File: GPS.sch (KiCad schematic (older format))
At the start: 6 parts, among them U5 MAX-M8

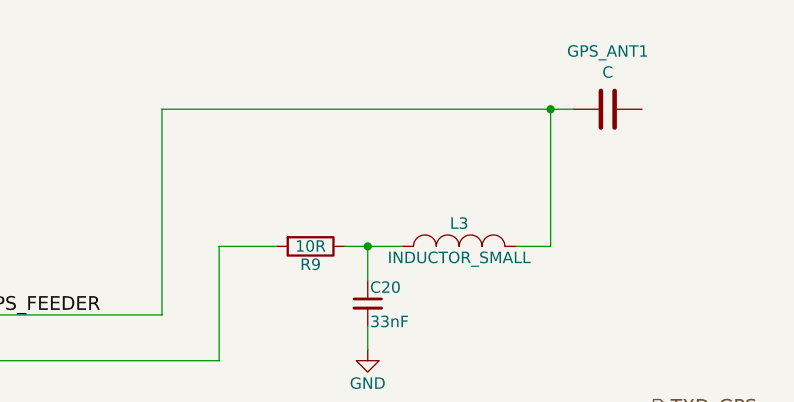
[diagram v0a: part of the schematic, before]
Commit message: Added edge-mount SMAs
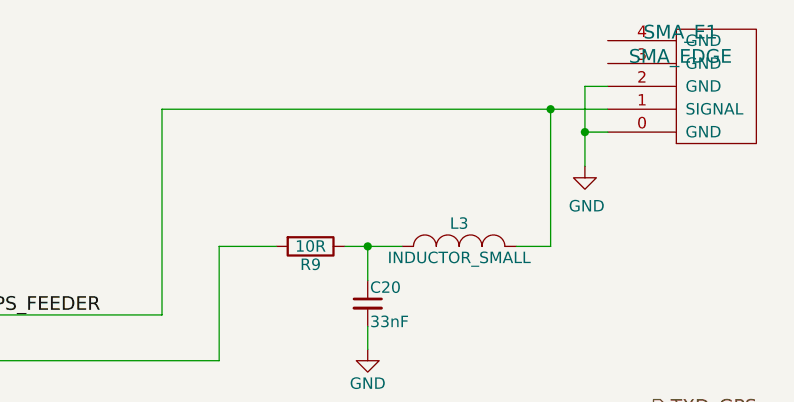
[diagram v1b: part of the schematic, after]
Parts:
- removed GPS_ANT1: C, Capacitors_SMD:C_1206, symbol C
- added SMA_E1: SMA_EDGE, SMA_EDGE:SMA_EDGE, symbol SMA_EDGE
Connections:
- net GND: now also SMA_E1.0 (GND), SMA_E1.2 (GND)
- net GPS_FEEDER: now also SMA_E1.1 (SIGNAL)
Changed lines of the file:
@@
 LIBS:miniultrapro
 LIBS:texas-instruments
+LIBS:sma_edge
 LIBS:lorawan_gps-cache
 EELAYER 25 0
@@
 	1    0    0    -1
 $EndComp
-$Comp
-L C GPS_ANT1
-U 1 1 56DB5A9C
-P 7050 2600
-F 0 "GPS_ANT1" V 6797 2600 50  0000 C CNN
-F 1 "C" V 6889 2600 50  0000 C CNN
-F 2 "Capacitors_SMD:C_1206" H 7088 2450 50  0001 C CNN
-F 3 "" H 7050 2600 50  0000 C CNN
-F 4 "1575AT43A40" V 7050 2600 60  0001 C CNN "MPN"
-	1    7050 2600
-	0    1    1    0
-$EndComp
 Text Label 4300 3500 0    60   ~ 0
 GPS_FEEDER
 $Comp
-L GND #PWR032
+L GND #PWR033
 U 1 1 56E9952A
 P 2700 5250
-F 0 "#PWR032" H 2700 5000 50  0001 C CNN
+F 0 "#PWR033" H 2700 5000 50  0001 C CNN
 F 1 "GND" H 2700 5100 50  0000 C CNN
 F 2 "" H 2700 5250 50  0000 C CNN
@@
 	1    0    0    -1
 $EndComp
-Wire Wire Line
-	2700 4700 2950 4700
-Wire Wire Line
-	2700 4650 2700 5250
-Wire Wire Line
-	2950 4800 2700 4800
-Connection ~ 2700 4800
-Wire Wire Line
-	2950 4900 2700 4900
-Connection ~ 2700 4900
 NoConn ~ 4250 4500
 NoConn ~ 4250 4900
@@
 NoConn ~ 2950 4150
 $Comp
-L +3.3V #PWR033
+L +3.3V #PWR034
 U 1 1 56E99604
 P 2700 3200
-F 0 "#PWR033" H 2700 3050 50  0001 C CNN
+F 0 "#PWR034" H 2700 3050 50  0001 C CNN
 F 1 "+3.3V" H 2700 3340 50  0000 C CNN
 F 2 "" H 2700 3200 50  0000 C CNN
@@
 	1    0    0    -1
 $EndComp
-Wire Wire Line
-	2700 4350 2950 4350
-Wire Wire Line
-	2700 3200 2700 4350
-Wire Wire Line
-	2950 3500 2700 3500
-Connection ~ 2700 3500
-Wire Wire Line
-	2950 3600 2700 3600
-Connection ~ 2700 3600
-Wire Wire Line
-	2950 3800 2700 3800
-Connection ~ 2700 3800
 $Comp
 L R R9
@@
 $EndComp
 $Comp
-L GND #PWR034
+L GND #PWR035
 U 1 1 56E99D41
 P 6000 3650
-F 0 "#PWR034" H 6000 3400 50  0001 C CNN
+F 0 "#PWR035" H 6000 3400 50  0001 C CNN
 F 1 "GND" H 6000 3500 50  0000 C CNN
 F 2 "" H 6000 3650 50  0000 C CNN
@@
 	1    0    0    -1
 $EndComp
-Connection ~ 2700 4350
-Connection ~ 2700 4700
-Wire Wire Line
-	4250 3500 5100 3500
-Wire Wire Line
-	5100 3500 5100 2600
-Wire Wire Line
-	5100 2600 6900 2600
-Wire Wire Line
-	6650 3200 6800 3200
-Wire Wire Line
-	6800 3200 6800 2600
-Connection ~ 6800 2600
-Wire Wire Line
-	5900 3200 6150 3200
-Wire Wire Line
-	5600 3200 5350 3200
-Wire Wire Line
-	5350 3200 5350 3700
-Wire Wire Line
-	5350 3700 4250 3700
-Wire Wire Line
-	6000 3350 6000 3200
-Connection ~ 6000 3200
-Wire Wire Line
-	6000 3650 6000 3550
-Wire Wire Line
-	4250 3900 7250 3900
-Wire Wire Line
-	4250 4000 7250 4000
-Wire Wire Line
-	4250 4200 7250 4200
-Wire Wire Line
-	4250 4300 7250 4300
 Text HLabel 7250 3900 2    60   Output ~ 0
 TXD_GPS
@@
 Text HLabel 7250 4300 2    60   Input ~ 0
 SCL_GPS
+$Comp
+L SMA_EDGE SMA_E1
+U 1 1 56F50EC5
+P 7400 2600
+F 0 "SMA_E1" H 7368 2263 60  0000 C CNN
+F 1 "SMA_EDGE" H 7368 2369 60  0000 C CNN
+F 2 "SMA_EDGE:SMA_EDGE" H 7400 2600 60  0001 C CNN
+F 3 "" H 7400 2600 60  0000 C CNN
+	1    7400 2600
+	1    0    0    1
+$EndComp
+Wire Wire Line
+	2700 4700 2950 4700
+Wire Wire Line
+	2700 4650 2700 5250
+Wire Wire Line
+	2950 4800 2700 4800
+Connection ~ 2700 4800
+Wire Wire Line
+	2950 4900 2700 4900
+Connection ~ 2700 4900
+Wire Wire Line
+	2700 4350 2950 4350
+Wire Wire Line
+	2700 3200 2700 4350
+Wire Wire Line
+	2950 3500 2700 3500
+Connection ~ 2700 3500
+Wire Wire Line
+	2950 3600 2700 3600
+Connection ~ 2700 3600
+Wire Wire Line
+	2950 3800 2700 3800
+Connection ~ 2700 3800
+Connection ~ 2700 4350
+Connection ~ 2700 4700
+Wire Wire Line
+	4250 3500 5100 3500
+Wire Wire Line
+	5100 3500 5100 2600
+Wire Wire Line
+	5100 2600 7050 2600
+Wire Wire Line
+	6650 3200 6800 3200
+Wire Wire Line
+	6800 3200 6800 2600
+Connection ~ 6800 2600
+Wire Wire Line
+	5900 3200 6150 3200
+Wire Wire Line
+	5600 3200 5350 3200
+Wire Wire Line
+	5350 3200 5350 3700
+Wire Wire Line
+	5350 3700 4250 3700
+Wire Wire Line
+	6000 3350 6000 3200
+Connection ~ 6000 3200
+Wire Wire Line
+	6000 3650 6000 3550
+Wire Wire Line
+	4250 3900 7250 3900
+Wire Wire Line
+	4250 4000 7250 4000
+Wire Wire Line
+	4250 4200 7250 4200
+Wire Wire Line
+	4250 4300 7250 4300
+$Comp
+L GND #PWR036
+U 1 1 56F511BA
+P 6950 2850
+F 0 "#PWR036" H 6950 2600 50  0001 C CNN
+F 1 "GND" H 6958 2676 50  0000 C CNN
+F 2 "" H 6950 2850 50  0000 C CNN
+F 3 "" H 6950 2850 50  0000 C CNN
+	1    6950 2850
+	1    0    0    -1
+$EndComp
+Wire Wire Line
+	7050 2500 6950 2500
+Wire Wire Line
+	6950 2500 6950 2850
+Wire Wire Line
+	7050 2700 6950 2700
+Connection ~ 6950 2700
 $EndSCHEMATC

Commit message: Changed L3 to 0603, L2 to 3x3, Fixed P8 silk and made gerbers
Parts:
- L3: footprint Capacitors_SMD:C_0805 -> Capacitors_SMD:C_0603
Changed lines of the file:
@@
 GPS_FEEDER
 $Comp
-L GND #PWR34
+L GND #PWR034
 U 1 1 56E9952A
 P 2700 5250
-F 0 "#PWR34" H 2700 5000 50  0001 C CNN
+F 0 "#PWR034" H 2700 5000 50  0001 C CNN
 F 1 "GND" H 2700 5100 50  0000 C CNN
 F 2 "" H 2700 5250 50  0000 C CNN
@@
 NoConn ~ 2950 4150
 $Comp
-L +3.3V #PWR33
+L +3.3V #PWR035
 U 1 1 56E99604
 P 2700 3200
-F 0 "#PWR33" H 2700 3050 50  0001 C CNN
+F 0 "#PWR035" H 2700 3050 50  0001 C CNN
 F 1 "+3.3V" H 2700 3340 50  0000 C CNN
 F 2 "" H 2700 3200 50  0000 C CNN
@@
 F 0 "L3" H 6400 3300 50  0000 C CNN
 F 1 "INDUCTOR_SMALL" H 6400 3150 50  0000 C CNN
-F 2 "Capacitors_SMD:C_0805" H 6400 3200 50  0001 C CNN
+F 2 "Capacitors_SMD:C_0603" H 6400 3200 50  0001 C CNN
 F 3 "" H 6400 3200 50  0000 C CNN
 	1    6400 3200
@@
 $EndComp
 $Comp
-L GND #PWR35
+L GND #PWR036
 U 1 1 56E99D41
 P 6000 3650
-F 0 "#PWR35" H 6000 3400 50  0001 C CNN
+F 0 "#PWR036" H 6000 3400 50  0001 C CNN
 F 1 "GND" H 6000 3500 50  0000 C CNN
 F 2 "" H 6000 3650 50  0000 C CNN
@@
 	4250 4300 7250 4300
 $Comp
-L GND #PWR36
+L GND #PWR037
 U 1 1 56F511BA
 P 6950 2850
-F 0 "#PWR36" H 6950 2600 50  0001 C CNN
+F 0 "#PWR037" H 6950 2600 50  0001 C CNN
 F 1 "GND" H 6958 2676 50  0000 C CNN
 F 2 "" H 6950 2850 50  0000 C CNN

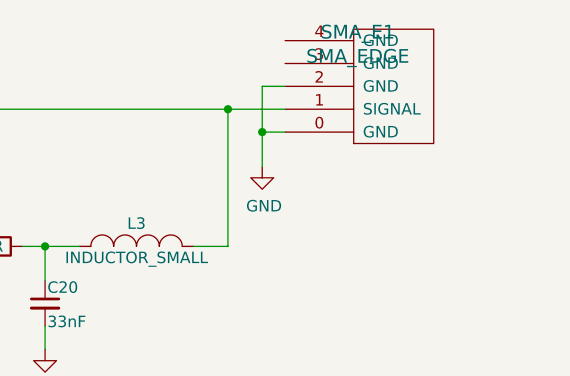
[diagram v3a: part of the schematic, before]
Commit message: Started changes after first round, micro usb connector, fixing footprint for accelerometer
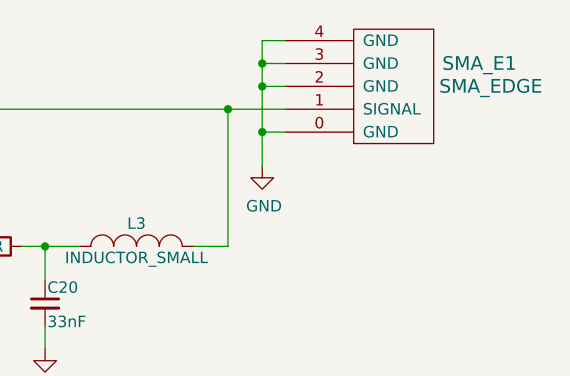
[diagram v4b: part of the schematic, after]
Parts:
- SMA_E1: footprint SMA_EDGE:SMA_EDGE -> edgemount_sma:SMA_EDGE
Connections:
- net GND: now also SMA_E1.3 (GND), SMA_E1.4 (GND)
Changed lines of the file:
@@
 U 1 1 56F50EC5
 P 7400 2600
-F 0 "SMA_E1" H 7368 2263 60  0000 C CNN
-F 1 "SMA_EDGE" H 7368 2369 60  0000 C CNN
-F 2 "SMA_EDGE:SMA_EDGE" H 7400 2600 60  0001 C CNN
+F 0 "SMA_E1" H 7900 2400 60  0000 C CNN
+F 1 "SMA_EDGE" H 7950 2500 60  0000 C CNN
+F 2 "edgemount_sma:SMA_EDGE" H 7400 2600 60  0001 C CNN
 F 3 "" H 7400 2600 60  0000 C CNN
 	1    7400 2600
@@
 	7050 2500 6950 2500
 Wire Wire Line
-	6950 2500 6950 2850
+	6950 2300 6950 2850
 Wire Wire Line
 	7050 2700 6950 2700
 Connection ~ 6950 2700
+Wire Wire Line
+	7050 2300 6950 2300
+Connection ~ 6950 2500
+Wire Wire Line
+	7050 2400 6950 2400
+Connection ~ 6950 2400
 $EndSCHEMATC

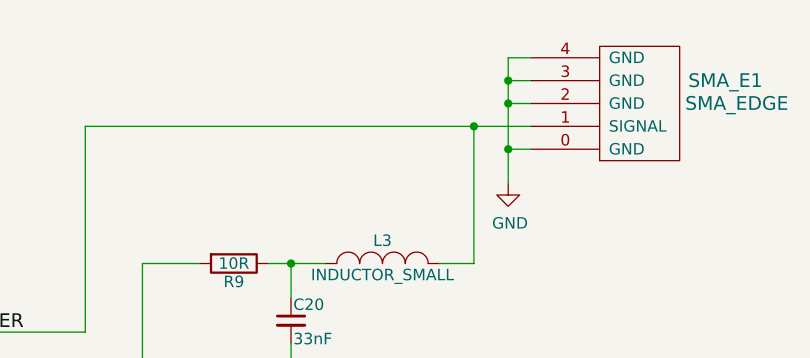
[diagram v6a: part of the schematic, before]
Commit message: Added dielectric antennae, finished wiring, DRC pass, no unconnects
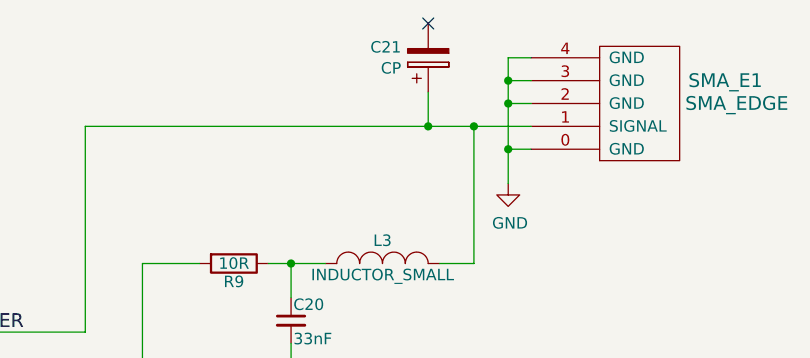
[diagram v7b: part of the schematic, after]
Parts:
- added C21: CP, Johanson:1575AT43A0040, symbol CP
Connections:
- net GPS_FEEDER: now also C21.1
- no-connect marks 5 -> 6
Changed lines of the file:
@@
 	7050 2400 6950 2400
 Connection ~ 6950 2400
+$Comp
+L CP C21
+U 1 1 57314782
+P 6600 2300
+F 0 "C21" H 6482 2254 50  0000 R CNN
+F 1 "CP" H 6482 2346 50  0000 R CNN
+F 2 "Johanson:1575AT43A0040" H 6638 2150 50  0001 C CNN
+F 3 "" H 6600 2300 50  0000 C CNN
+	1    6600 2300
+	1    0    0    1
+$EndComp
+Connection ~ 6600 2600
+Wire Wire Line
+	6600 2450 6600 2600
+NoConn ~ 6600 2150
 $EndSCHEMATC
